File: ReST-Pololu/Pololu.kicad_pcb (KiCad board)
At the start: 2 copper layers, 12 parts, among them P1 02X07-MALE, P2 01X03-MALE, P3 03-SCREW-TERM, P4 01X03-MALE, P5 02-SCREW-TERM, P6 02X04-MALE, P7 02X03-MALE, U1 POLOLU_A4988

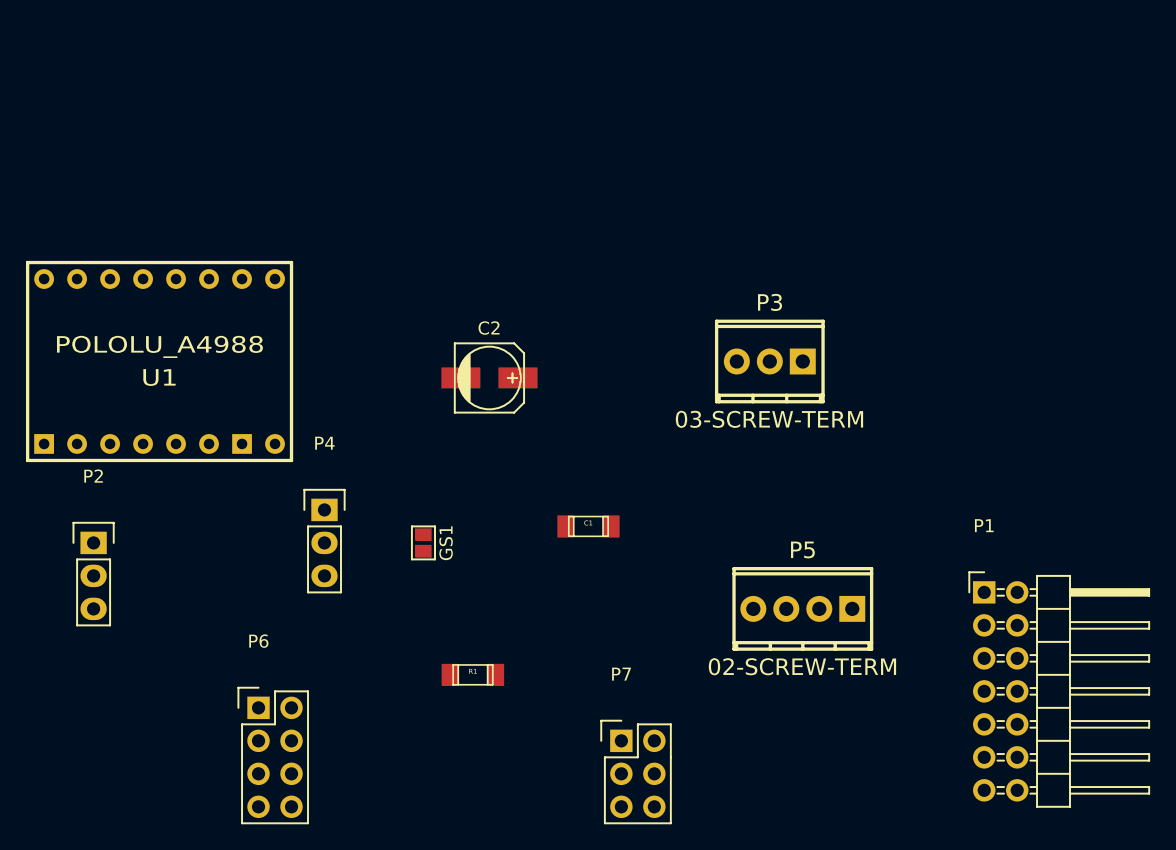
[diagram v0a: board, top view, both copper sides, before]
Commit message: Added Pololu Driver PCB
Size is 3.5cm * 3.75cm
Im pretty happy with that size
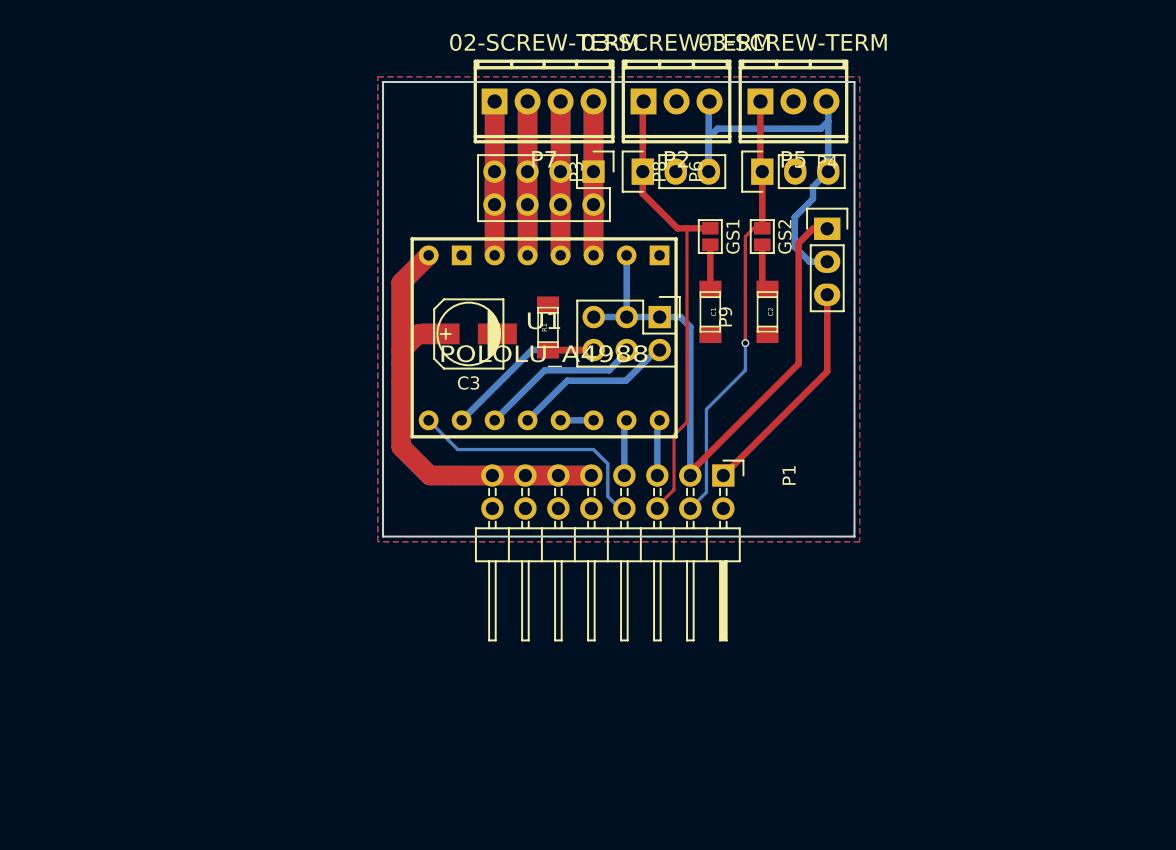
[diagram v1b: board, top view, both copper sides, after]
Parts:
- added C1: 100nF, ok-smd-generic:1206, F.Cu at (165.6, 80.0)
- added GS1: GS2, Connect:GS2, F.Cu at (165.6, 74.2)
- added P2: 03-SCREW-TERM, 2:mpt_0,5%2f3-2,54, F.Cu at (163.0, 63.8)
- added P3: 01X03-MALE, Pin_Headers:Pin_Header_Straight_1x03, F.Cu at (160.4, 69.2)
- P1: value 02X07-MALE -> CONN_02X08; footprint Pin_Headers:Pin_Header_Angled_2x07 -> Pin_Headers:Pin_Header_Angled_2x08
- moved P4 61.5 mm to (174.6, 73.6)
- moved P8 48.7 mm to (156.6, 69.2), turned to 270 degrees
- moved P7 43.9 mm to (152.8, 63.8), turned to 180 degrees
- moved P6 42.6 mm to (169.6, 69.2), turned to 90 degrees
- moved GS2 35.2 mm to (169.6, 74.2)
- moved P9 32.8 mm to (161.7, 80.4), turned to 270 degrees
- moved U1 29.7 mm to (152.8, 82.0), turned to 180 degrees
- moved R1 27.4 mm to (153.1, 81.2), turned to 90 degrees
- moved P1 22.0 mm to (166.6, 92.6), turned to 270 degrees
- moved C2 21.5 mm to (170.0, 80.0), turned to 270 degrees
- moved P5 20.1 mm to (172.0, 63.8), turned to 180 degrees
- moved C3 3.74 mm to (147.0, 81.7), turned to 180 degrees
- renumbered C1 to C2, C2 to C3, GS1 to GS2, P2 to P4, P3 to P5, P4 to P6, P5 to P7, P6 to P8, P7 to P9
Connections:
- GS2 pad 1: /STOP -> /STOP-MIN
- P1 pad 1: GND -> +5V
- P1 pad 10: +3V3 -> GND
- P1 pad 11: /EN -> +12V
- P1 pad 12: /STEP -> GND
- P1 pad 13: /STOP -> +12V
- P1 pad 14: /DIR -> GND
- P1 pad 2: +12V -> (no net)
- P1 pad 3: GND -> +3V3
- P1 pad 4: +12V -> /STOP-MIN
- P1 pad 5: GND -> /DIR
- P1 pad 6: +12V -> /STOP-MAX
- P1 pad 7: GND -> /STEP
- P1 pad 8: +12V -> /EN
- P1 pad 9: +5V -> +12V
- P4 pad 2: Net-(P2-Pad2) -> Net-(P2-Pad3)
- P5 pad 1: Net-(P2-Pad2) -> /STOP-MIN
- P5 pad 3: /STOP -> Net-(P2-Pad3)
- P6 pad 1: Net-(P2-Pad2) -> /STOP-MIN
- P6 pad 3: /STOP -> Net-(P2-Pad3)
- P9 pad 1: Net-(P7-Pad1) (its old number) -> +3V3
- P9 pad 2: +3V3 -> Net-(P9-Pad2)
- P9 pad 3: Net-(P7-Pad3) (its old number) -> +3V3
- P9 pad 4: +3V3 -> Net-(P9-Pad4)
- P9 pad 5: Net-(P7-Pad5) -> +3V3
- P9 pad 6: +3V3 -> Net-(P9-Pad6)
- R1 pad 1: Net-(P7-Pad5) -> Net-(P9-Pad6)
- U1 pad 10: Net-(P7-Pad5) -> Net-(P9-Pad6)
- U1 pad 11: Net-(P7-Pad3) (its old number) -> Net-(P9-Pad4)
- U1 pad 12: Net-(P7-Pad1) (its old number) -> Net-(P9-Pad2)
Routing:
- net +12V: track 0.00 -> 67.0 mm
- net +3V3: track 0.00 -> 48.0 mm
- net /STOP-MAX: track 0.00 -> 36.1 mm
- net /STOP-MIN: track 0.00 -> 34.1 mm, vias 0 -> 1
- net Net-(P2-Pad3): track 0.00 -> 33.1 mm
- net Net-(P7-Pad4): track 0.00 -> 23.8 mm
- net Net-(P7-Pad1): track 0.00 -> 23.8 mm
- net Net-(P7-Pad3): track 0.00 -> 23.8 mm
- net Net-(P7-Pad2): track 0.00 -> 23.8 mm
- net /EN: track 0.00 -> 19.3 mm
- net +5V: track 0.00 -> 17.2 mm
- net Net-(P9-Pad6): track 0.00 -> 15.9 mm
- net Net-(P9-Pad4): track 0.00 -> 12.5 mm
- net Net-(P9-Pad2): track 0.00 -> 12.4 mm
- net /STEP: track 0.00 -> 4.32 mm
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- added copper zone on B.Cu, net GND
- added copper zone on F.Cu, net GND
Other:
- board outline added: 36.3 x 35 mm

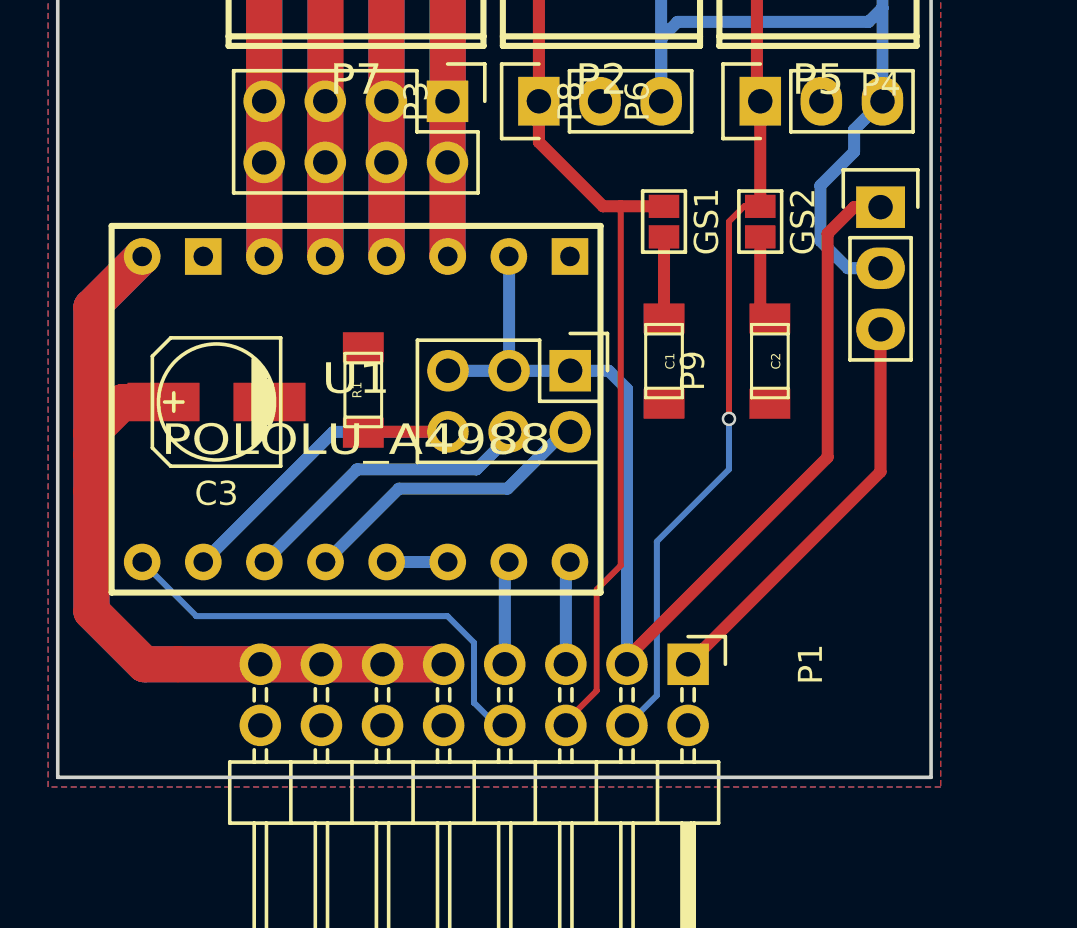
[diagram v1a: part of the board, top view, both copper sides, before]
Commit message: Changed minor issues in the Pololu Driver.
Heatbed wont get much smaller. Finished Dimensions:
Heatbed: 30,4mm * 47,8mm
Heater: 29mm * 34,1mm
Pololu: 36,3mm * 35,2mm
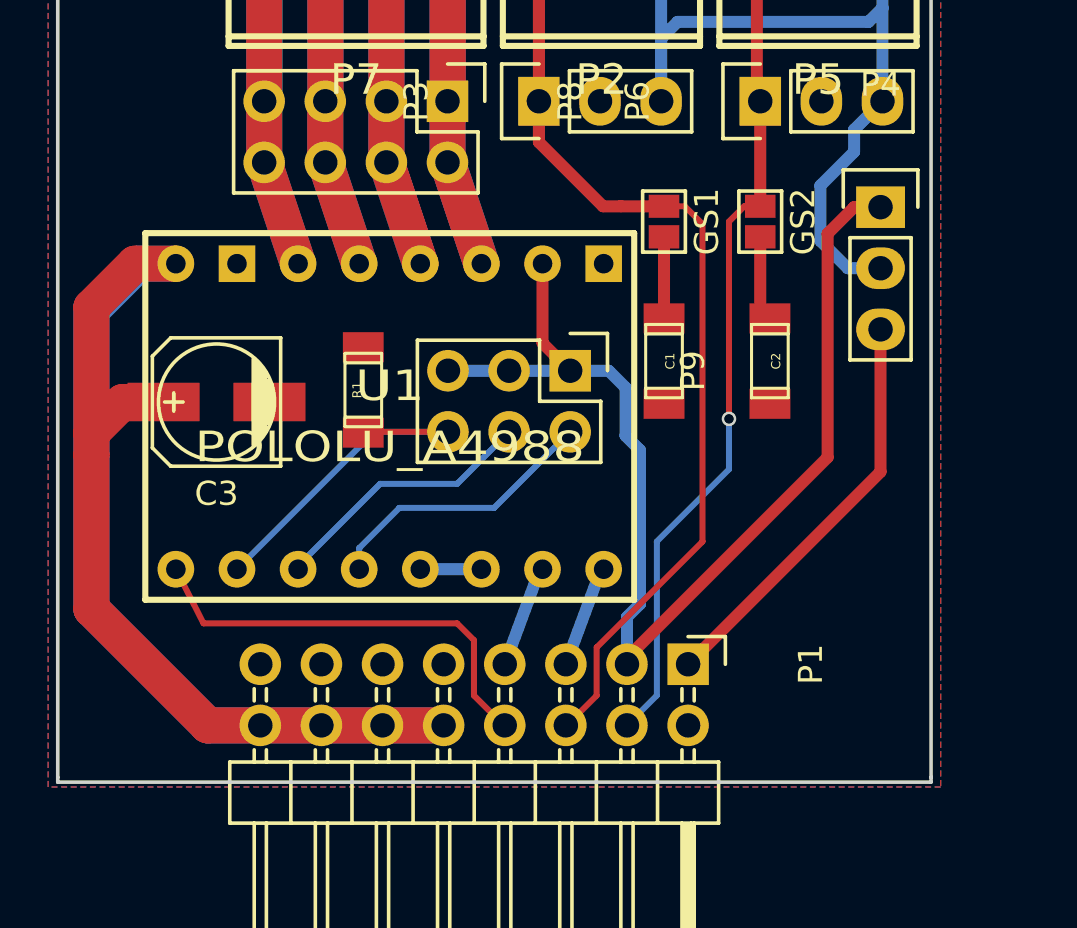
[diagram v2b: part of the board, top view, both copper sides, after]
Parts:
- moved U1 1.43 mm to (154.2, 82.3)
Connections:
- P1 pad 10: GND -> +12V
- P1 pad 11: +12V -> GND
- P1 pad 12: GND -> +12V
- P1 pad 13: +12V -> GND
- P1 pad 14: GND -> +12V
- P1 pad 15: +12V -> GND
- P1 pad 16: GND -> +12V
- P1 pad 9: +12V -> GND
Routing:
- net +12V: track 67.0 -> 71.6 mm
- net /STOP-MAX: track 36.1 -> 38.7 mm
- net Net-(P9-Pad4): track 12.5 -> 11.2 mm
- net Net-(P9-Pad6): track 15.9 -> 14.7 mm
- net /EN: track 19.3 -> 18.2 mm
- net Net-(P7-Pad2): track 23.8 -> 24.8 mm
- net Net-(P7-Pad3): track 23.8 -> 24.8 mm
- net Net-(P7-Pad4): track 23.8 -> 24.8 mm
- net Net-(P7-Pad1): track 23.8 -> 24.8 mm
- net Net-(P9-Pad2): track 12.4 -> 11.7 mm
- net +3V3: track 48.0 -> 48.6 mm
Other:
- board size 36.3 x 35 mm -> 36.3 x 35.2 mm
